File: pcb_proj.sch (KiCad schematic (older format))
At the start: 0 parts

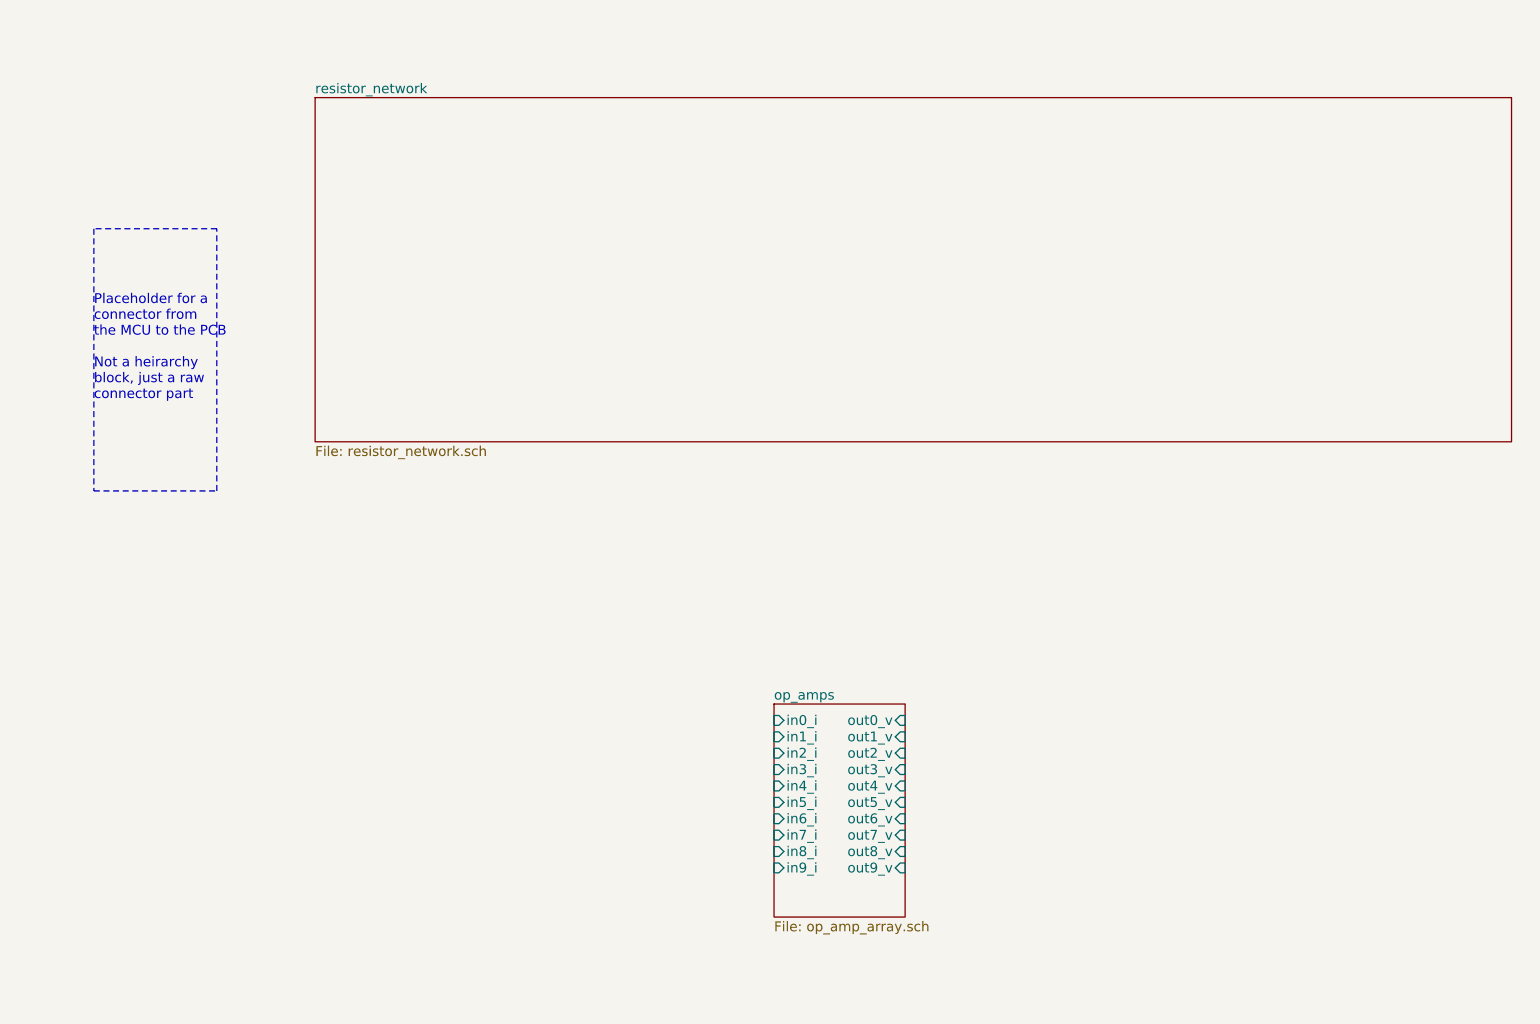
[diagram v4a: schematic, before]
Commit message: Added some wires
Added some wires, placed some terminals. Just a little bit of work.
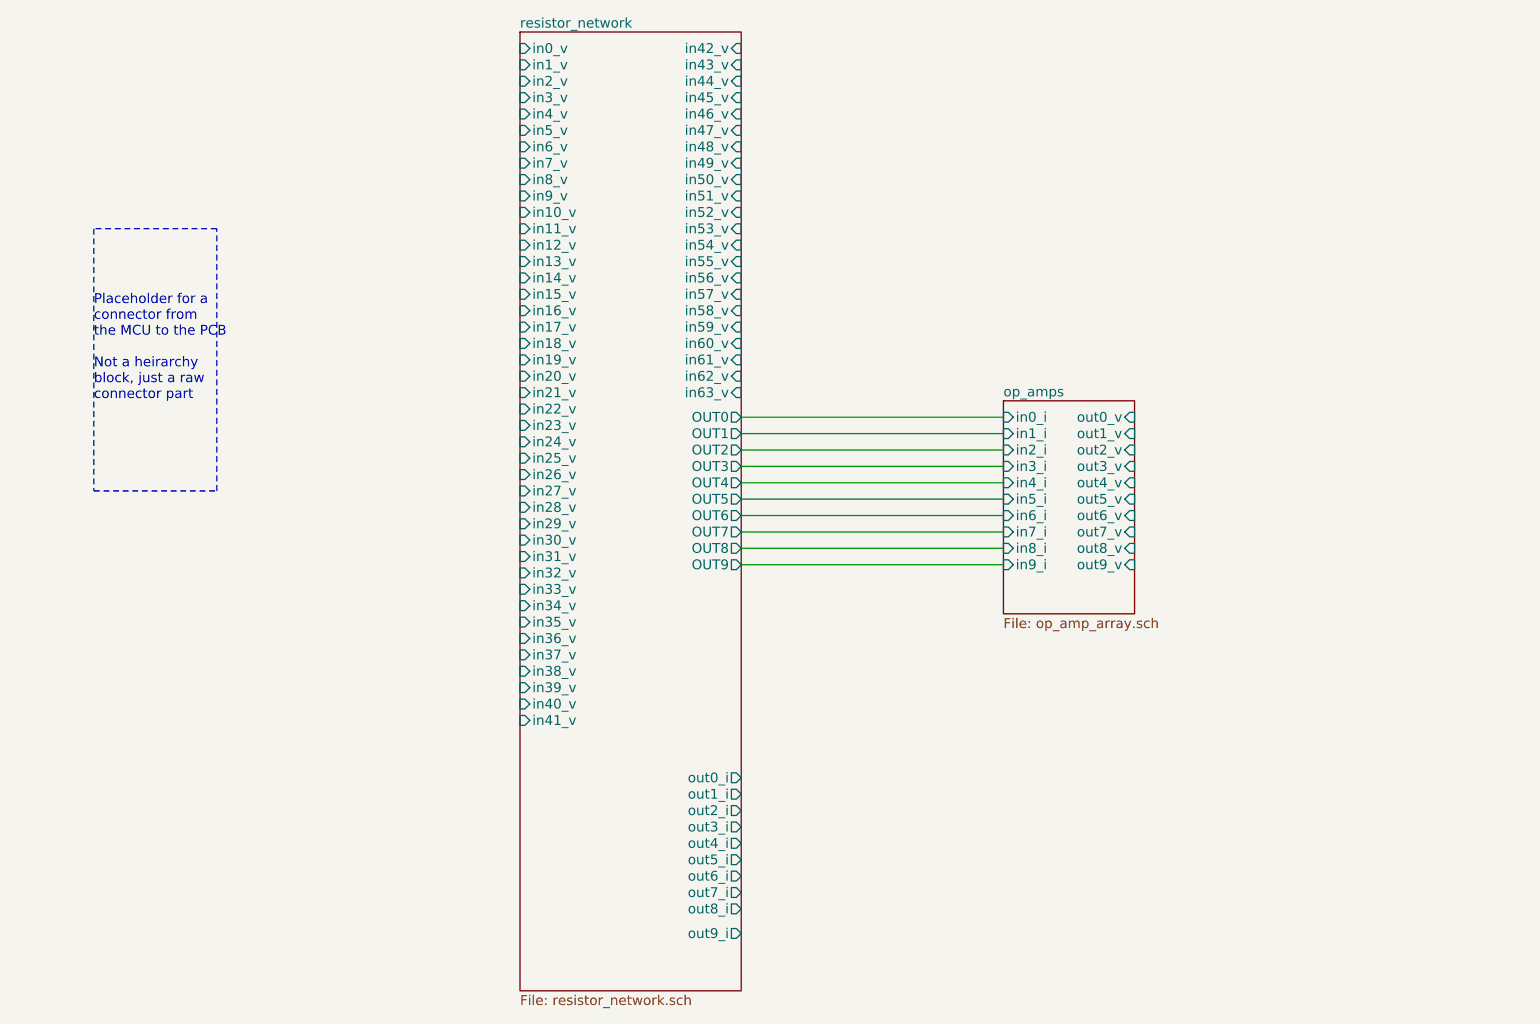
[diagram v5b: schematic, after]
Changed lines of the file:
@@
 $EndDescr
 $Sheet
-S 5300 4950 800  1300
+S 6700 3100 800  1300
 U 5C6B8575
 F0 "op_amps" 60
 F1 "op_amp_array.sch" 60
-F2 "in0_i" I L 5300 5050 60
-F3 "in1_i" I L 5300 5150 60
-F4 "in2_i" I L 5300 5250 60
-F5 "in3_i" I L 5300 5350 60
-F6 "in4_i" I L 5300 5450 60
-F7 "in9_i" I L 5300 5950 60
-F8 "in8_i" I L 5300 5850 60
-F9 "in7_i" I L 5300 5750 60
-F10 "in6_i" I L 5300 5650 60
-F11 "in5_i" I L 5300 5550 60
-F12 "out0_v" I R 6100 5050 60
-F13 "out1_v" I R 6100 5150 60
-F14 "out2_v" I R 6100 5250 60
-F15 "out3_v" I R 6100 5350 60
-F16 "out4_v" I R 6100 5450 60
-F17 "out5_v" I R 6100 5550 60
-F18 "out6_v" I R 6100 5650 60
-F19 "out7_v" I R 6100 5750 60
-F20 "out8_v" I R 6100 5850 60
-F21 "out9_v" I R 6100 5950 60
+F2 "in0_i" I L 6700 3200 60
+F3 "in1_i" I L 6700 3300 60
+F4 "in2_i" I L 6700 3400 60
+F5 "in3_i" I L 6700 3500 60
+F6 "in4_i" I L 6700 3600 60
+F7 "in9_i" I L 6700 4100 60
+F8 "in8_i" I L 6700 4000 60
+F9 "in7_i" I L 6700 3900 60
+F10 "in6_i" I L 6700 3800 60
+F11 "in5_i" I L 6700 3700 60
+F12 "out0_v" I R 7500 3200 60
+F13 "out1_v" I R 7500 3300 60
+F14 "out2_v" I R 7500 3400 60
+F15 "out3_v" I R 7500 3500 60
+F16 "out4_v" I R 7500 3600 60
+F17 "out5_v" I R 7500 3700 60
+F18 "out6_v" I R 7500 3800 60
+F19 "out7_v" I R 7500 3900 60
+F20 "out8_v" I R 7500 4000 60
+F21 "out9_v" I R 7500 4100 60
 $EndSheet
 Wire Notes Line
@@
 Placeholder for a\nconnector from\nthe MCU to the PCB\n\nNot a heirarchy\nblock, just a raw\nconnector part
 $Sheet
-S 2500 1250 7300 2100
+S 3750 850  1350 5850
 U 5C6B8B3B
 F0 "resistor_network" 60
 F1 "resistor_network.sch" 60
+F2 "in0_v" I L 3750 950 60
+F3 "in1_v" I L 3750 1050 60
+F4 "in2_v" I L 3750 1150 60
+F5 "in3_v" I L 3750 1250 60
+F6 "in4_v" I L 3750 1350 60
+F7 "in5_v" I L 3750 1450 60
+F8 "in6_v" I L 3750 1550 60
+F9 "in7_v" I L 3750 1650 60
+F10 "in8_v" I L 3750 1750 60
+F11 "in9_v" I L 3750 1850 60
+F12 "in10_v" I L 3750 1950 60
+F13 "in11_v" I L 3750 2050 60
+F14 "in12_v" I L 3750 2150 60
+F15 "in13_v" I L 3750 2250 60
+F16 "in14_v" I L 3750 2350 60
+F17 "in15_v" I L 3750 2450 60
+F18 "in16_v" I L 3750 2550 60
+F19 "in17_v" I L 3750 2650 60
+F20 "in18_v" I L 3750 2750 60
+F21 "in19_v" I L 3750 2850 60
+F22 "in20_v" I L 3750 2950 60
+F23 "in21_v" I L 3750 3050 60
+F24 "in22_v" I L 3750 3150 60
+F25 "in23_v" I L 3750 3250 60
+F26 "in24_v" I L 3750 3350 60
+F27 "in25_v" I L 3750 3450 60
+F28 "in26_v" I L 3750 3550 60
+F29 "in27_v" I L 3750 3650 60
+F30 "in28_v" I L 3750 3750 60
+F31 "in29_v" I L 3750 3850 60
+F32 "in30_v" I L 3750 3950 60
+F33 "in31_v" I L 3750 4050 60
+F34 "out1_i" O R 5100 5500 60
+F35 "out2_i" O R 5100 5600 60
+F36 "out3_i" O R 5100 5700 60
+F37 "out4_i" O R 5100 5800 60
+F38 "out5_i" O R 5100 5900 60
+F39 "out6_i" O R 5100 6000 60
+F40 "out7_i" O R 5100 6100 60
+F41 "out8_i" O R 5100 6200 60
+F42 "out9_i" O R 5100 6350 60
+F43 "out0_i" O R 5100 5400 60
+F44 "in32_v" I L 3750 4150 60
+F45 "in33_v" I L 3750 4250 60
+F46 "in34_v" I L 3750 4350 60
+F47 "in35_v" I L 3750 4450 60
+F48 "in36_v" I L 3750 4550 60
+F49 "in37_v" I L 3750 4650 60
+F50 "in38_v" I L 3750 4750 60
+F51 "in39_v" I L 3750 4850 60
+F52 "in40_v" I L 3750 4950 60
+F53 "in41_v" I L 3750 5050 60
+F54 "in42_v" I R 5100 950 60
+F55 "in43_v" I R 5100 1050 60
+F56 "in44_v" I R 5100 1150 60
+F57 "in45_v" I R 5100 1250 60
+F58 "in46_v" I R 5100 1350 60
+F59 "in47_v" I R 5100 1450 60
+F60 "in49_v" I R 5100 1650 60
+F61 "in48_v" I R 5100 1550 60
+F62 "in50_v" I R 5100 1750 60
+F63 "in51_v" I R 5100 1850 60
+F64 "in52_v" I R 5100 1950 60
+F65 "in53_v" I R 5100 2050 60
+F66 "in54_v" I R 5100 2150 60
+F67 "in55_v" I R 5100 2250 60
+F68 "in56_v" I R 5100 2350 60
+F69 "in57_v" I R 5100 2450 60
+F70 "in58_v" I R 5100 2550 60
+F71 "in59_v" I R 5100 2650 60
+F72 "in60_v" I R 5100 2750 60
+F73 "in61_v" I R 5100 2850 60
+F74 "in62_v" I R 5100 2950 60
+F75 "in63_v" I R 5100 3050 60
+F76 "OUT0" O R 5100 3200 60
+F77 "OUT1" O R 5100 3300 60
+F78 "OUT2" O R 5100 3400 60
+F79 "OUT3" O R 5100 3500 60
+F80 "OUT4" O R 5100 3600 60
+F81 "OUT5" O R 5100 3700 60
+F82 "OUT6" O R 5100 3800 60
+F83 "OUT7" O R 5100 3900 60
+F84 "OUT8" O R 5100 4000 60
+F85 "OUT9" O R 5100 4100 60
 $EndSheet
+Wire Wire Line
+	5100 3200 6700 3200
+Wire Wire Line
+	5100 3300 6700 3300
+Wire Wire Line
+	5100 3400 6700 3400
+Wire Wire Line
+	5100 3500 6700 3500
+Wire Wire Line
+	6700 3600 5100 3600
+Wire Wire Line
+	5100 3700 6700 3700
+Wire Wire Line
+	5100 3800 6700 3800
+Wire Wire Line
+	6700 3900 5100 3900
+Wire Wire Line
+	5100 4000 6700 4000
+Wire Wire Line
+	6700 4100 5100 4100
 $EndSCHEMATC

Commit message: Updated resistors 32-63
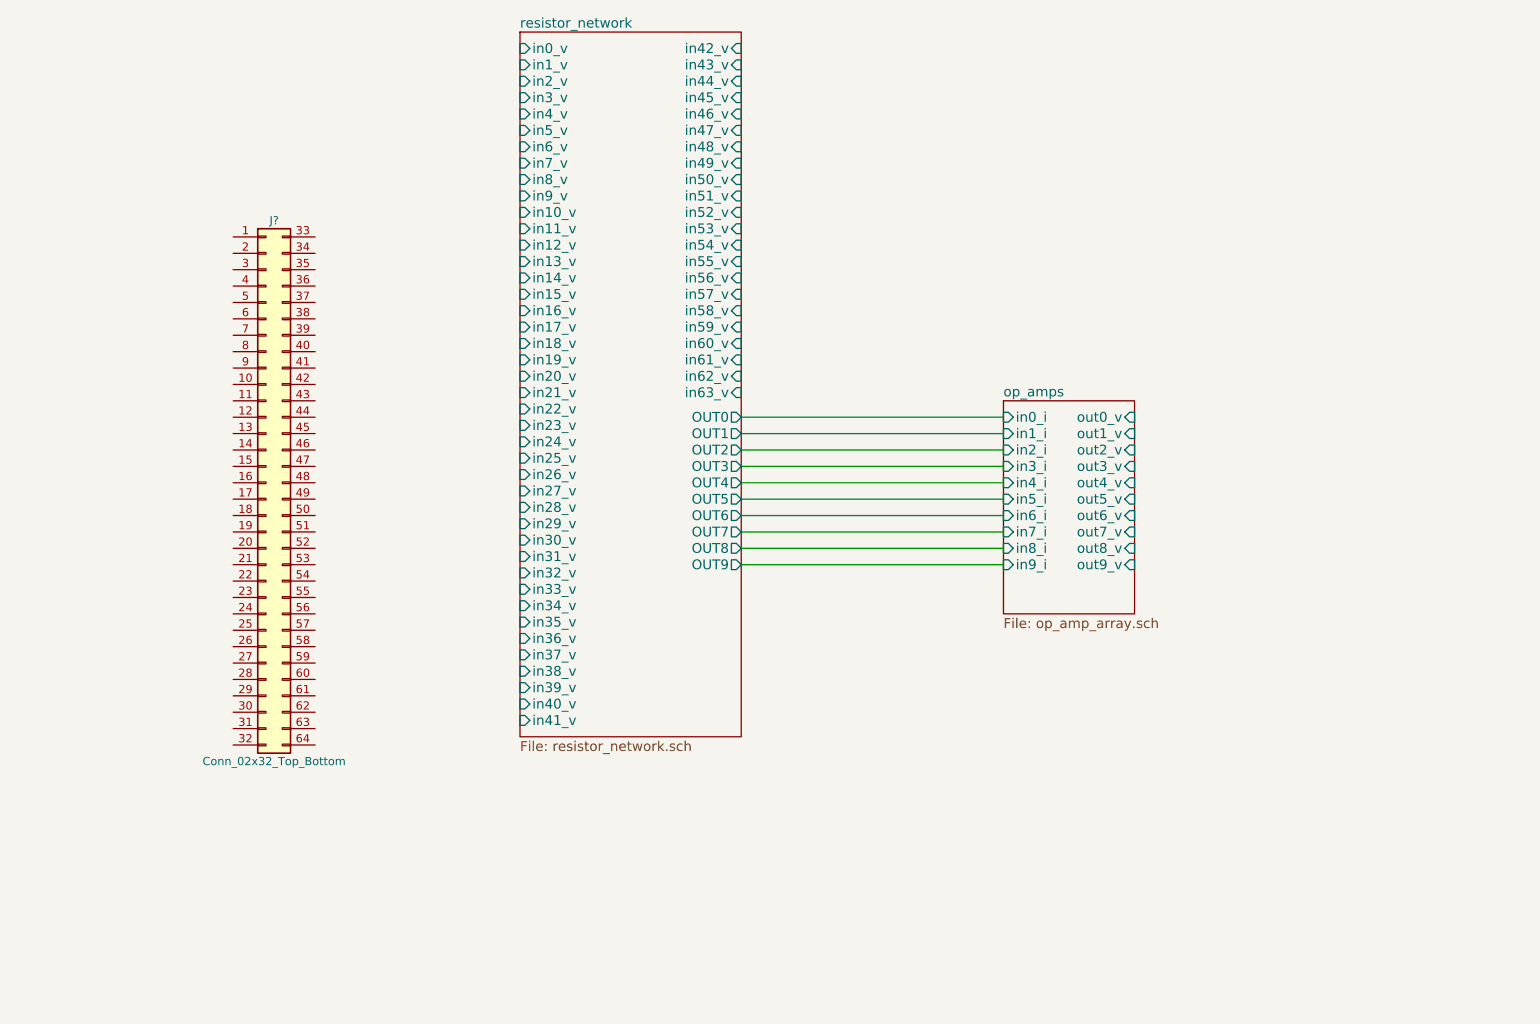
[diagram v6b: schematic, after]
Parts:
- added J?: Conn_02x32_Top_Bottom, symbol Conn_02x32_Top_Bottom
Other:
- note removed: "Placeholder for a\nconnector from\nthe MCU to the PCB\n\nNot a heirarchy\nblock, just a raw\nconnector part"
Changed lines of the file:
@@
 F21 "out9_v" I R 7500 4100 60
 $EndSheet
-Wire Notes Line
-	1150 2050 1150 3650
-Wire Notes Line
-	1150 3650 1900 3650
-Wire Notes Line
-	1900 3650 1900 2050
-Wire Notes Line
-	1900 2050 1150 2050
-Text Notes 1150 3100 0    60   ~ 0
-Placeholder for a\nconnector from\nthe MCU to the PCB\n\nNot a heirarchy\nblock, just a raw\nconnector part
 $Sheet
-S 3750 850  1350 5850
+S 3750 850  1350 4300
 U 5C6B8B3B
 F0 "resistor_network" 60
@@
 F32 "in30_v" I L 3750 3950 60
 F33 "in31_v" I L 3750 4050 60
-F34 "out1_i" O R 5100 5500 60
-F35 "out2_i" O R 5100 5600 60
-F36 "out3_i" O R 5100 5700 60
-F37 "out4_i" O R 5100 5800 60
-F38 "out5_i" O R 5100 5900 60
-F39 "out6_i" O R 5100 6000 60
-F40 "out7_i" O R 5100 6100 60
-F41 "out8_i" O R 5100 6200 60
-F42 "out9_i" O R 5100 6350 60
-F43 "out0_i" O R 5100 5400 60
-F44 "in32_v" I L 3750 4150 60
-F45 "in33_v" I L 3750 4250 60
-F46 "in34_v" I L 3750 4350 60
-F47 "in35_v" I L 3750 4450 60
-F48 "in36_v" I L 3750 4550 60
-F49 "in37_v" I L 3750 4650 60
-F50 "in38_v" I L 3750 4750 60
-F51 "in39_v" I L 3750 4850 60
-F52 "in40_v" I L 3750 4950 60
-F53 "in41_v" I L 3750 5050 60
-F54 "in42_v" I R 5100 950 60
-F55 "in43_v" I R 5100 1050 60
-F56 "in44_v" I R 5100 1150 60
-F57 "in45_v" I R 5100 1250 60
-F58 "in46_v" I R 5100 1350 60
-F59 "in47_v" I R 5100 1450 60
-F60 "in49_v" I R 5100 1650 60
-F61 "in48_v" I R 5100 1550 60
-F62 "in50_v" I R 5100 1750 60
-F63 "in51_v" I R 5100 1850 60
-F64 "in52_v" I R 5100 1950 60
-F65 "in53_v" I R 5100 2050 60
-F66 "in54_v" I R 5100 2150 60
-F67 "in55_v" I R 5100 2250 60
-F68 "in56_v" I R 5100 2350 60
-F69 "in57_v" I R 5100 2450 60
-F70 "in58_v" I R 5100 2550 60
-F71 "in59_v" I R 5100 2650 60
-F72 "in60_v" I R 5100 2750 60
-F73 "in61_v" I R 5100 2850 60
-F74 "in62_v" I R 5100 2950 60
-F75 "in63_v" I R 5100 3050 60
-F76 "OUT0" O R 5100 3200 60
-F77 "OUT1" O R 5100 3300 60
-F78 "OUT2" O R 5100 3400 60
-F79 "OUT3" O R 5100 3500 60
-F80 "OUT4" O R 5100 3600 60
-F81 "OUT5" O R 5100 3700 60
-F82 "OUT6" O R 5100 3800 60
-F83 "OUT7" O R 5100 3900 60
-F84 "OUT8" O R 5100 4000 60
-F85 "OUT9" O R 5100 4100 60
+F34 "in32_v" I L 3750 4150 60
+F35 "in33_v" I L 3750 4250 60
+F36 "in34_v" I L 3750 4350 60
+F37 "in35_v" I L 3750 4450 60
+F38 "in36_v" I L 3750 4550 60
+F39 "in37_v" I L 3750 4650 60
+F40 "in38_v" I L 3750 4750 60
+F41 "in39_v" I L 3750 4850 60
+F42 "in40_v" I L 3750 4950 60
+F43 "in41_v" I L 3750 5050 60
+F44 "in42_v" I R 5100 950 60
+F45 "in43_v" I R 5100 1050 60
+F46 "in44_v" I R 5100 1150 60
+F47 "in45_v" I R 5100 1250 60
+F48 "in46_v" I R 5100 1350 60
+F49 "in47_v" I R 5100 1450 60
+F50 "in49_v" I R 5100 1650 60
+F51 "in48_v" I R 5100 1550 60
+F52 "in50_v" I R 5100 1750 60
+F53 "in51_v" I R 5100 1850 60
+F54 "in52_v" I R 5100 1950 60
+F55 "in53_v" I R 5100 2050 60
+F56 "in54_v" I R 5100 2150 60
+F57 "in55_v" I R 5100 2250 60
+F58 "in56_v" I R 5100 2350 60
+F59 "in57_v" I R 5100 2450 60
+F60 "in58_v" I R 5100 2550 60
+F61 "in59_v" I R 5100 2650 60
+F62 "in60_v" I R 5100 2750 60
+F63 "in61_v" I R 5100 2850 60
+F64 "in62_v" I R 5100 2950 60
+F65 "in63_v" I R 5100 3050 60
+F66 "OUT0" O R 5100 3200 60
+F67 "OUT1" O R 5100 3300 60
+F68 "OUT2" O R 5100 3400 60
+F69 "OUT3" O R 5100 3500 60
+F70 "OUT4" O R 5100 3600 60
+F71 "OUT5" O R 5100 3700 60
+F72 "OUT6" O R 5100 3800 60
+F73 "OUT7" O R 5100 3900 60
+F74 "OUT8" O R 5100 4000 60
+F75 "OUT9" O R 5100 4100 60
 $EndSheet
 Wire Wire Line
@@
 Wire Wire Line
 	6700 4100 5100 4100
+$Comp
+L Conn_02x32_Top_Bottom J?
+U 1 1 5C80365B
+P 2200 3600
+F 0 "J?" H 2250 5200 50  0000 C CNN
+F 1 "Conn_02x32_Top_Bottom" H 2250 1900 50  0000 C CNN
+F 2 "" H 2200 3600 50  0001 C CNN
+F 3 "" H 2200 3600 50  0001 C CNN
+	1    2200 3600
+	1    0    0    -1
+$EndComp
 $EndSCHEMATC

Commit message: Added footprints, finished schematic, began PCB layout
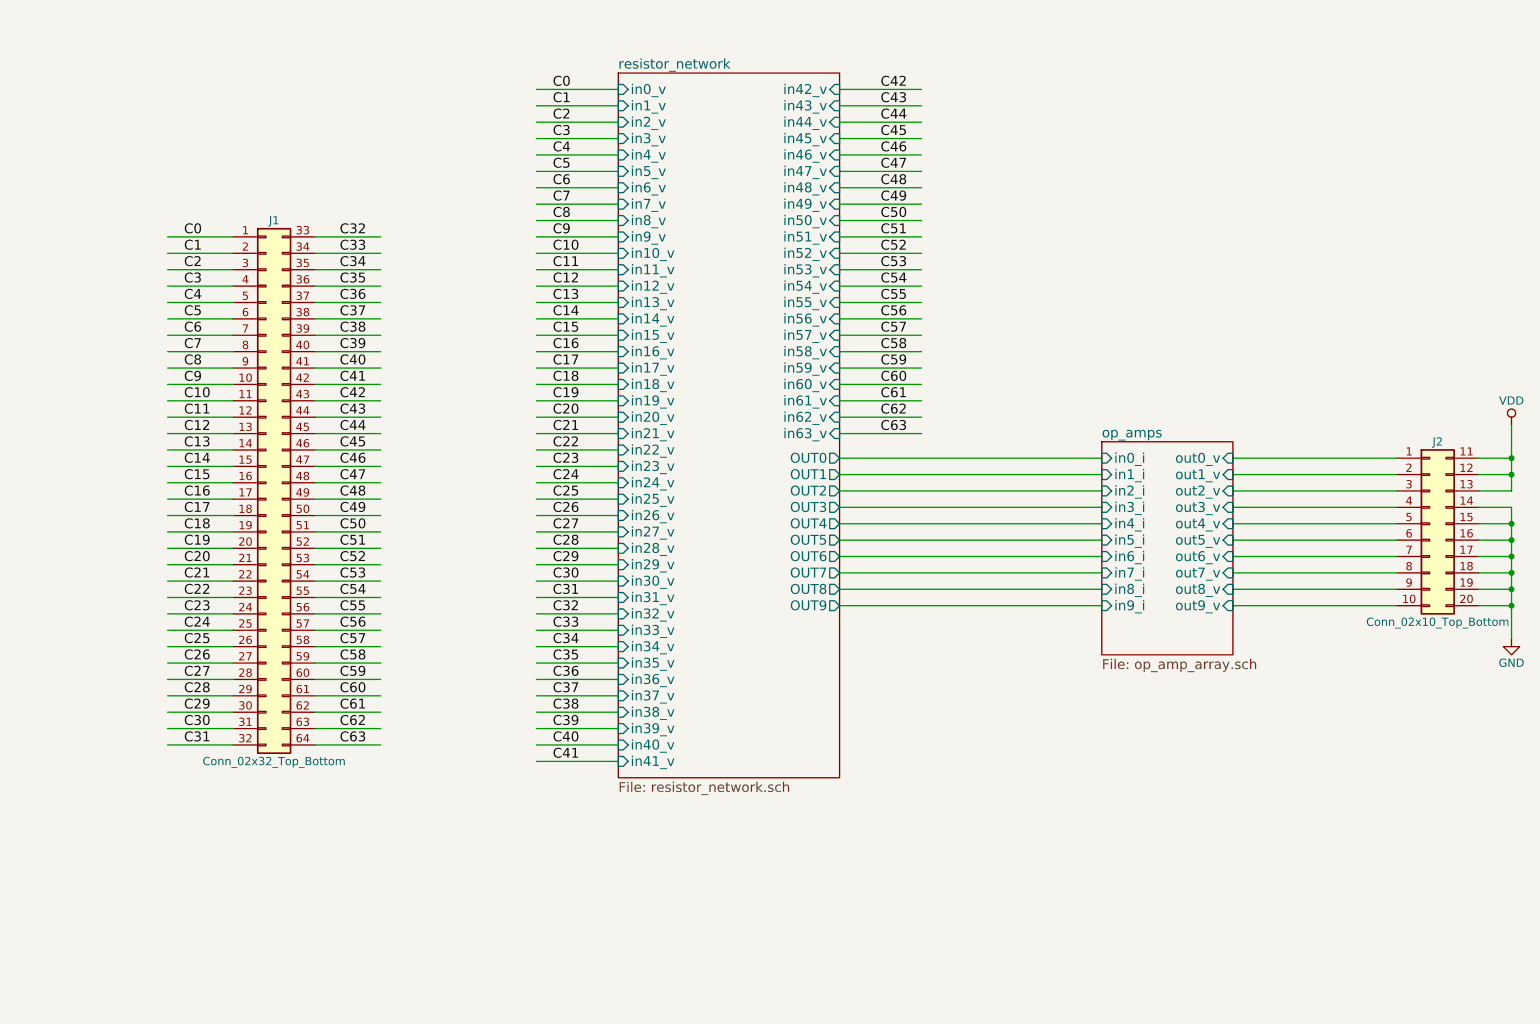
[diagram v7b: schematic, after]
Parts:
- added J2: Conn_02x10_Top_Bottom, Connector_PinHeader_1.00mm:PinHeader_2x10_P1.00mm_Vertical, symbol Conn_02x10_Top_Bottom
- J1: renamed from J?; footprint (none) -> Connector_PinHeader_1.00mm:PinHeader_2x32_P1.00mm_Vertical
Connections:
- net labels added: C0, C1, C10, C11, C12, C13, C14, C15, C16, C17, C18, C19, C2, C20, C21, C22, C23, C24, C25, C26, C27, C28, C29, C3, C30, C31, C32, C33, C34, C35, C36, C37, C38, C39, C4, C40, C41, C42, C43, C44, C45, C46, C47, C48, C49, C5, C50, C51, C52, C53, C54, C55, C56, C57, C58, C59, C6, C60, C61, C62, C63, C7, C8, C9, GND, VDD
- wire segments 10 -> 160
